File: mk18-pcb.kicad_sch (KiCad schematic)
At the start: 98 parts, among them J10 Conn_02x07_Top_Bottom, J17 Conn_01x06_Socket, J18 Conn_01x06_Socket, J19 Conn_01x06_Socket, J20 Conn_01x06_Socket, J7 Conn_02x06_Top_Bottom, J8 Conn_02x07_Top_Bottom, J9 Conn_02x06_Top_Bottom, P1 FH26W-13S-0_3SHW(60), P10 FH26W-13S-0_3SHW(60), P11 FH26W-13S-0_3SHW(60), P2 FH26W-13S-0_3SHW(60), P3 FH26W-13S-0_3SHW(60), P4 FH26W-13S-0_3SHW(60), P5 FH26W-13S-0_3SHW(60), P6 FH26W-13S-0_3SHW(60), P7 FH26W-13S-0_3SHW(60), P8 FH26W-13S-0_3SHW(60), P9 FH26W-13S-0_3SHW(60), T1 Conn_01x01_Socket, T10 Conn_01x01_Socket, T2 Conn_01x01_Socket, T3 Conn_01x01_Socket, T4 Conn_01x01_Socket, T5 Conn_01x01_Socket, T6 Conn_01x01_Socket, T7 Conn_01x01_Socket, T8 Conn_01x01_Socket, T9 Conn_01x01_Socket, U1 TYPE-C-31-M-12, U10 1N4148W_C81598, U11 1N4148W_C81598, U12 1N4148W_C81598, U13 1N4148W_C81598, U14 1N4148W_C81598, U15 1N4148W_C81598, U16 ECT818001569, U17 HC-FPC-05-10-16RLTAG, U2 AZC199-04S-MS, U3 1N4148W_C81598, U4 1N4148W_C81598, U4 SN74LVC1T45DRL, U5 1N4148W_C81598, U6 1N4148W_C81598, U7 1N4148W_C81598, U9 1N4148W_C81598

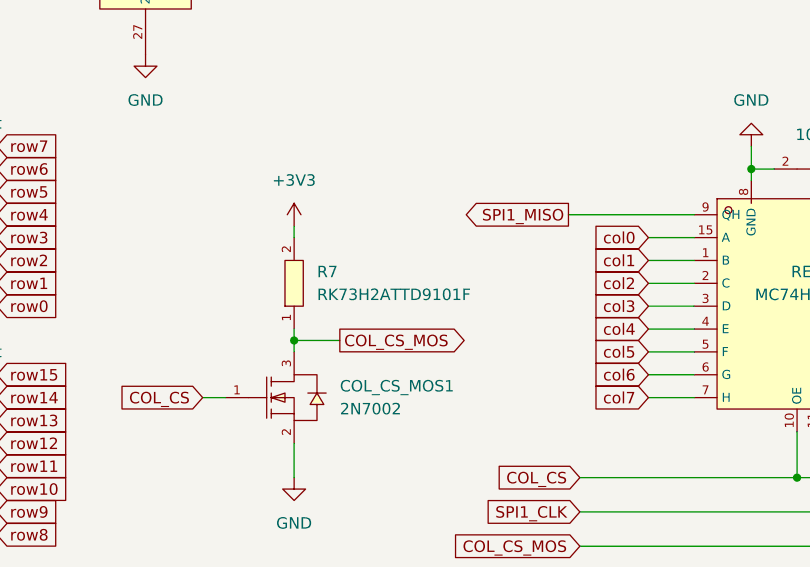
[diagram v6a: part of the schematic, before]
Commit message: replace two parts
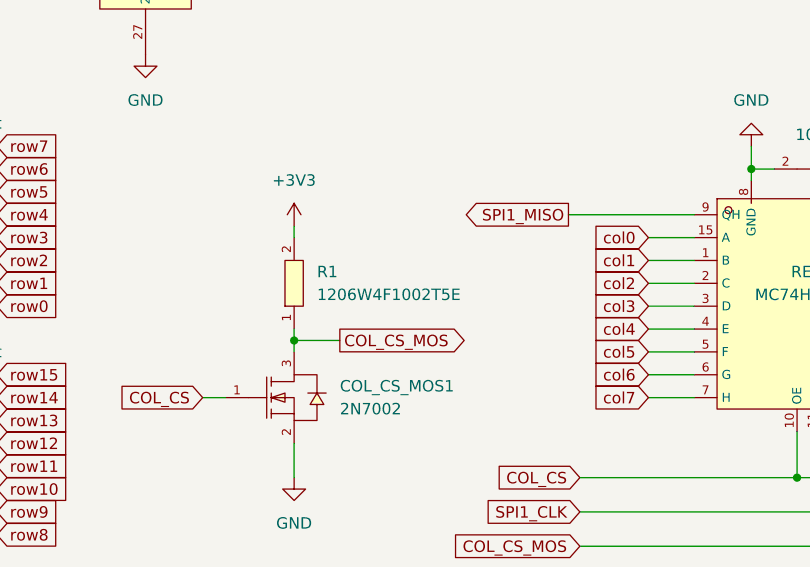
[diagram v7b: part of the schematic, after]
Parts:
- removed R7: RK73H2ATTD9101F, ct-kicad:R0805, symbol ct-kicad:RK73H2ATTD9101F
- added R1: 1206W4F1002T5E, ct-kicad:R1206, symbol ct-kicad:1206W4F1002T5E
- CYBOARD-MACRO1: footprint ct-kicad:FPC-SMD_16P-P0.50_HCTL_HC-FPC-05-10-16RLTAG -> ct-kicad:FPC-SMD_16P-P0.50_HDGC_0.5K-A-16PBF
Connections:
- net +3V3: now also R1.2
- net COL_CS_MOS: now also R1.1
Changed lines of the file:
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@@
     )
   )
+  (symbol (lib_id "ct-kicad:1206W4F1002T5E") (at 303.53 259.08 90) (unit 1)
+    (in_bom yes) (on_board yes) (dnp no) (fields_autoplaced)
+    (property "Reference" "R1" (at 306.07 257.81 90)
+      (effects (font (size 1.27 1.27)) (justify right))
+    )
+    (property "Value" "1206W4F1002T5E" (at 306.07 260.35 90)
+      (effects (font (size 1.27 1.27)) (justify right))
+    )
+    (property "Footprint" "ct-kicad:R1206" (at 313.69 259.08 0)
+      (effects (font (size 1.27 1.27) italic) hide)
+    )
+    (property "Datasheet" "https://item.szlcsc.com/311874.html" (at 303.403 261.366 0)
+      (effects (font (size 1.27 1.27)) (justify left) hide)
+    )
+    (property "LCSC" "C17902" (at 303.53 259.08 0)
+      (effects (font (size 1.27 1.27)) hide)
+    )
+    (pin "1")
+    (pin "2")
+    (instances
+      (project "mk18-pcb"
+        (path "/bb2be946-374e-4172-8486-a9a12db7ac7b"
+          (reference "R1") (unit 1)
+        )
+      )
+    )
+  )
   (symbol (lib_id "power:VCC") (at 566.42 91.44 0) (unit 1)
     (in_bom yes) (on_board yes) (dnp no) (fields_autoplaced)
@@
     )
   )
-  (symbol (lib_id "ct-kicad:RK73H2ATTD9101F") (at 303.53 259.08 90) (unit 1)
-    (in_bom yes) (on_board yes) (dnp no) (fields_autoplaced)
-    (property "Reference" "R7" (at 306.07 257.81 90)
-      (effects (font (size 1.27 1.27)) (justify right))
-    )
-    (property "Value" "RK73H2ATTD9101F" (at 306.07 260.35 90)
-      (effects (font (size 1.27 1.27)) (justify right))
-    )
-    (property "Footprint" "ct-kicad:R0805" (at 313.69 259.08 0)
-      (effects (font (size 1.27 1.27) italic) hide)
-    )
-    (property "Datasheet" "https://item.szlcsc.com/142685.html" (at 303.403 261.366 0)
-      (effects (font (size 1.27 1.27)) (justify left) hide)
-    )
-    (property "LCSC" "C317276" (at 303.53 259.08 0)
-      (effects (font (size 1.27 1.27)) hide)
-    )
-    (pin "1")
-    (pin "2")
-    (instances
-      (project "mk18-pcb"
-        (path "/bb2be946-374e-4172-8486-a9a12db7ac7b"
-          (reference "R7") (unit 1)
-        )
-      )
-    )
-  )
   (symbol (lib_id "power:VCC") (at 505.46 373.38 270) (unit 1)
     (in_bom yes) (on_board yes) (dnp no) (fields_autoplaced)
@@
       (effects (font (size 1.27 1.27)) (justify left))
     )
-    (property "Footprint" "ct-kicad:FPC-SMD_16P-P0.50_HCTL_HC-FPC-05-10-16RLTAG" (at 464.82 250.19 0)
+    (property "Footprint" "ct-kicad:FPC-SMD_16P-P0.50_HDGC_0.5K-A-16PBF" (at 464.82 250.19 0)
       (effects (font (size 1.27 1.27) italic) hide)
     )

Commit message: final commits, changing to some basic parts
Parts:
- removed J10, J8: Conn_02x07_Top_Bottom, Connector_PinHeader_2.54mm:PinHeader_2x07_P2.54mm_Vertical, symbol Connector_Generic:Conn_02x07_Top_Bottom
- removed J17, J18, J19, J20: Conn_01x06_Socket, Connector_JST:JST_XH_B6B-XH-A_1x06_P2.50mm_Vertical, symbol Connector:Conn_01x06_Socket
- removed J7, J9: Conn_02x06_Top_Bottom, Connector_PinSocket_2.54mm:PinSocket_2x06_P2.54mm_Vertical, symbol Connector_Generic:Conn_02x06_Top_Bottom
- removed U1: TYPE-C-31-M-12, kicad-library:USB-C_SMD-TYPE-C-31-M-12, symbol kicad-symbols:TYPE-C-31-M-12
- removed U10, U11, U12, U13, U14, U15, U9: 1N4148W_C81598, kicad-library:SOD-123F_L2.7-W1.6-LS3.8-RD, symbol kicad-symbols:1N4148W_C81598
- 5WAY1, ADC1, COL1, COL2, DBG1, FAL1, FAL2, G22, G3, G4, G6, G7, G8, H1, H2, H3, H4, IND1, LCD1, LED-EXT-DO1, LED-FAL1, LED-FAL2, LED-IND1, LED-MACRO1, PWM1, PWR-OUT1, RESET1, ROW1, ROW2, T1, T10, T2, T3, T4, T5, T6, T7, T8, T9: now left out of the parts list
- C1, C2, C3, C4, C5, C6: symbol ct-kicad:C0402X7R104K160NTB -> ct-kicad:CL05B104KO5NNNC; LCSC C115671 -> C1525
- MOSFET1: symbol kicad-symbols:AO3401A_C347476 -> ct-kicad:AO3401A; LCSC C347476 -> C15127
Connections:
- no-connect marks 31 -> 29
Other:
- note removed: "Falcon col-row selection jumpers"
- note removed: "Macropad"
- note removed: "Pedals USB-C connector"
- note removed: "RKJXT"
- moved on the sheet: C1, C2, C3, C4, C5, C6
